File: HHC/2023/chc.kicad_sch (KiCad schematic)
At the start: 9 parts

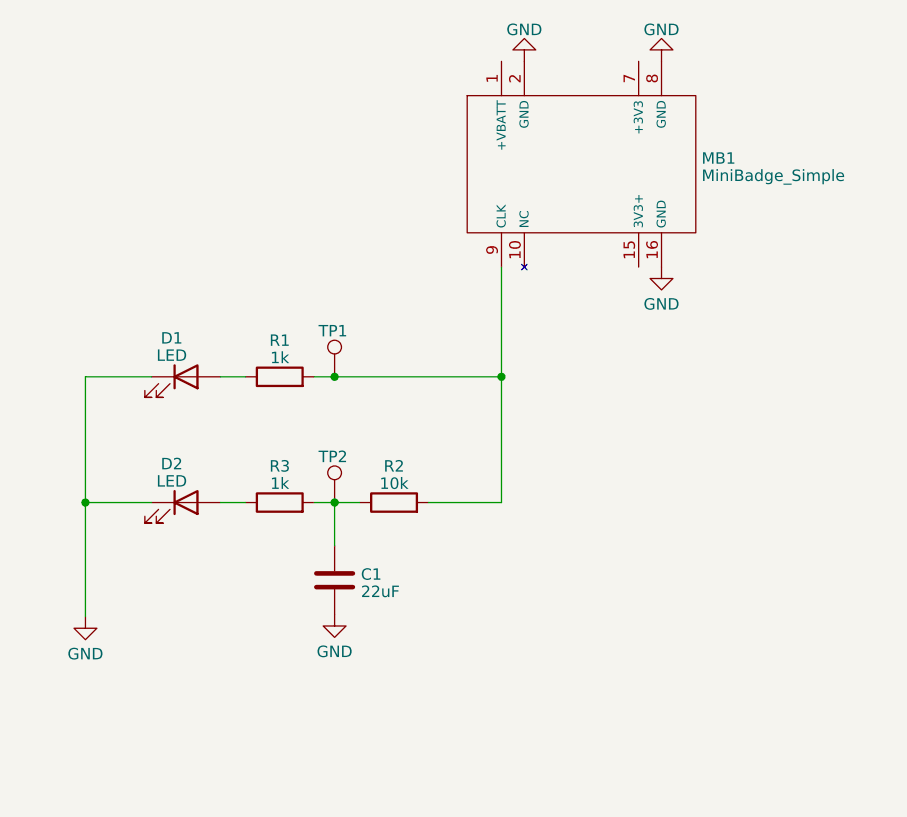
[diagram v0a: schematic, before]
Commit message: Added panel for the 2023 minibadge
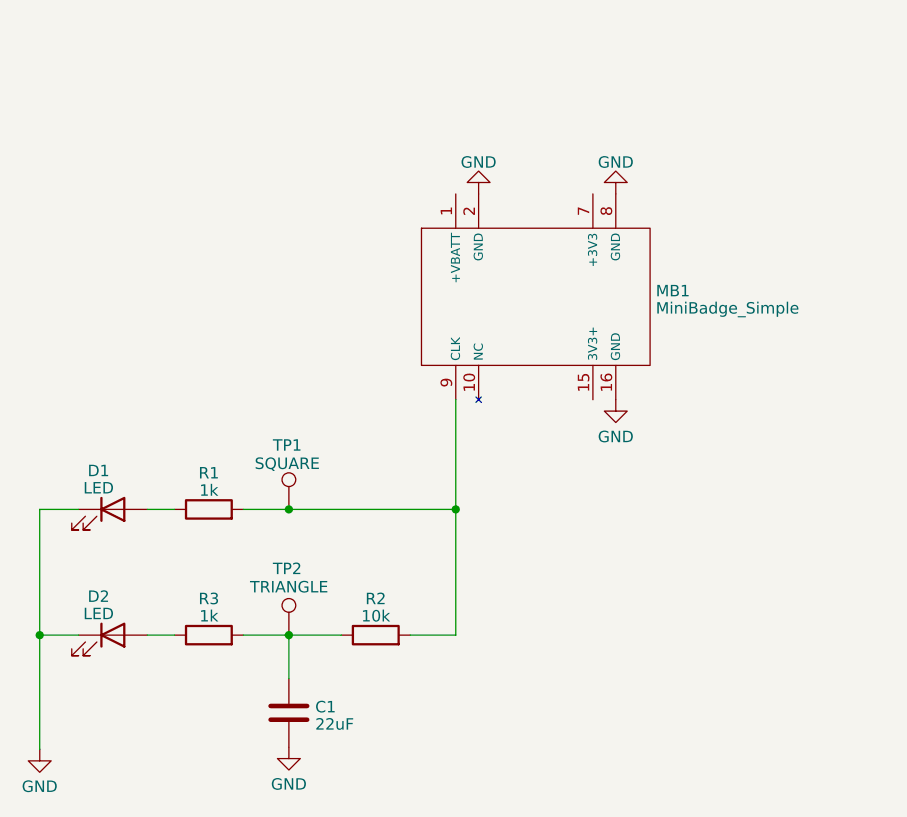
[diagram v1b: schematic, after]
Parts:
- TP1: value TestPoint -> SQUARE
- TP2: value TestPoint -> TRIANGLE
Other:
- company: (none) -> SAINTCON
- title: (none) -> Circuit Hacking Community Minibadge
- moved on the sheet: C1, D1, D2, MB1, R1, R2, R3, TP1, TP2
